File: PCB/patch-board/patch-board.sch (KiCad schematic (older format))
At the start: 104 parts, among them J1 USB_B, J11 AOUT1, J12 AOUT2, J13 AOUT3, J14 AOUT4, J15 AOUT5, J16 AOUT6, J17 AOUT7, J18 AOUT8, J2 LOGIC POWER SUPPLY, J21 DIGITAL OUT1, J22 DIGITAL OUT2, J23 DIGITAL OUT3, J24 DIGITAL OUT4, J3 MEGA_13-8, J31 S01, J32 S02, J33 S03, J34 S04, J35 S05, J36 S06, J37 S07, J38 S08, J39 S09, J4 MEGA_7-0, J40 S10, J41 SV, J42 SV, J43 SV, J44 SV, J45 SV, J46 SV, J5 MEGA_14-21, J6 MEGA_A8-A15, J7 MEGA_A0-A7, J8 MEGA_POWER, J9 MEGA_22-53, SW1 D1A, SW11 SW_DPST, SW12 SW_DPST, SW13 Conn_01x02, SW2 D1B, SW3 D2A, SW4 D2B, SW5 D3A, SW6 D3B, SW7 D4A, SW8 D4B, U1 74HC00, U10 74HC08, U11 74HC00, U12 74HC08, U13 74HC08, U2 74HC08, U3 74HC08, U4 74HC00, U5 74HC08, U6 74HC08, U7 74HC14, U8 74HC00, U9 74HC08

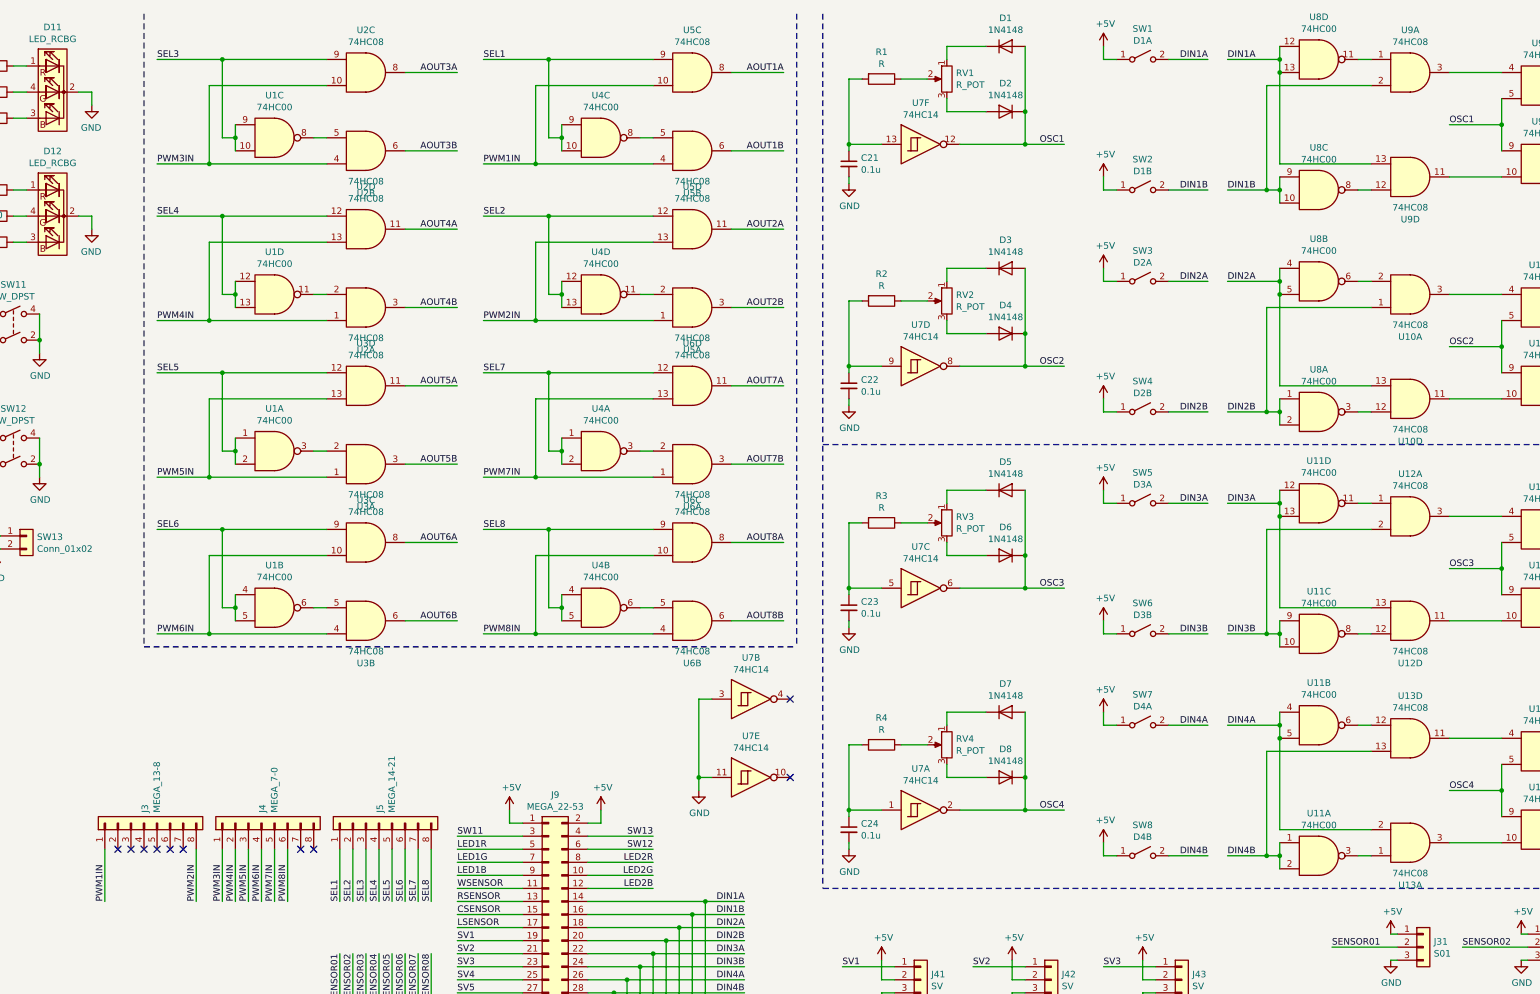
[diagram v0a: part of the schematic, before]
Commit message: D13 ピンの配線ミスを修正 AOUT5-8 のシルクミスを修正 U13 のユニット割り当てミスを修正
git-svn-id: https://shiro-home.ddns.net/svn/project/motor-driver/trunk@32 73406841-da20-4056-b287-c5b29fcc9b8e
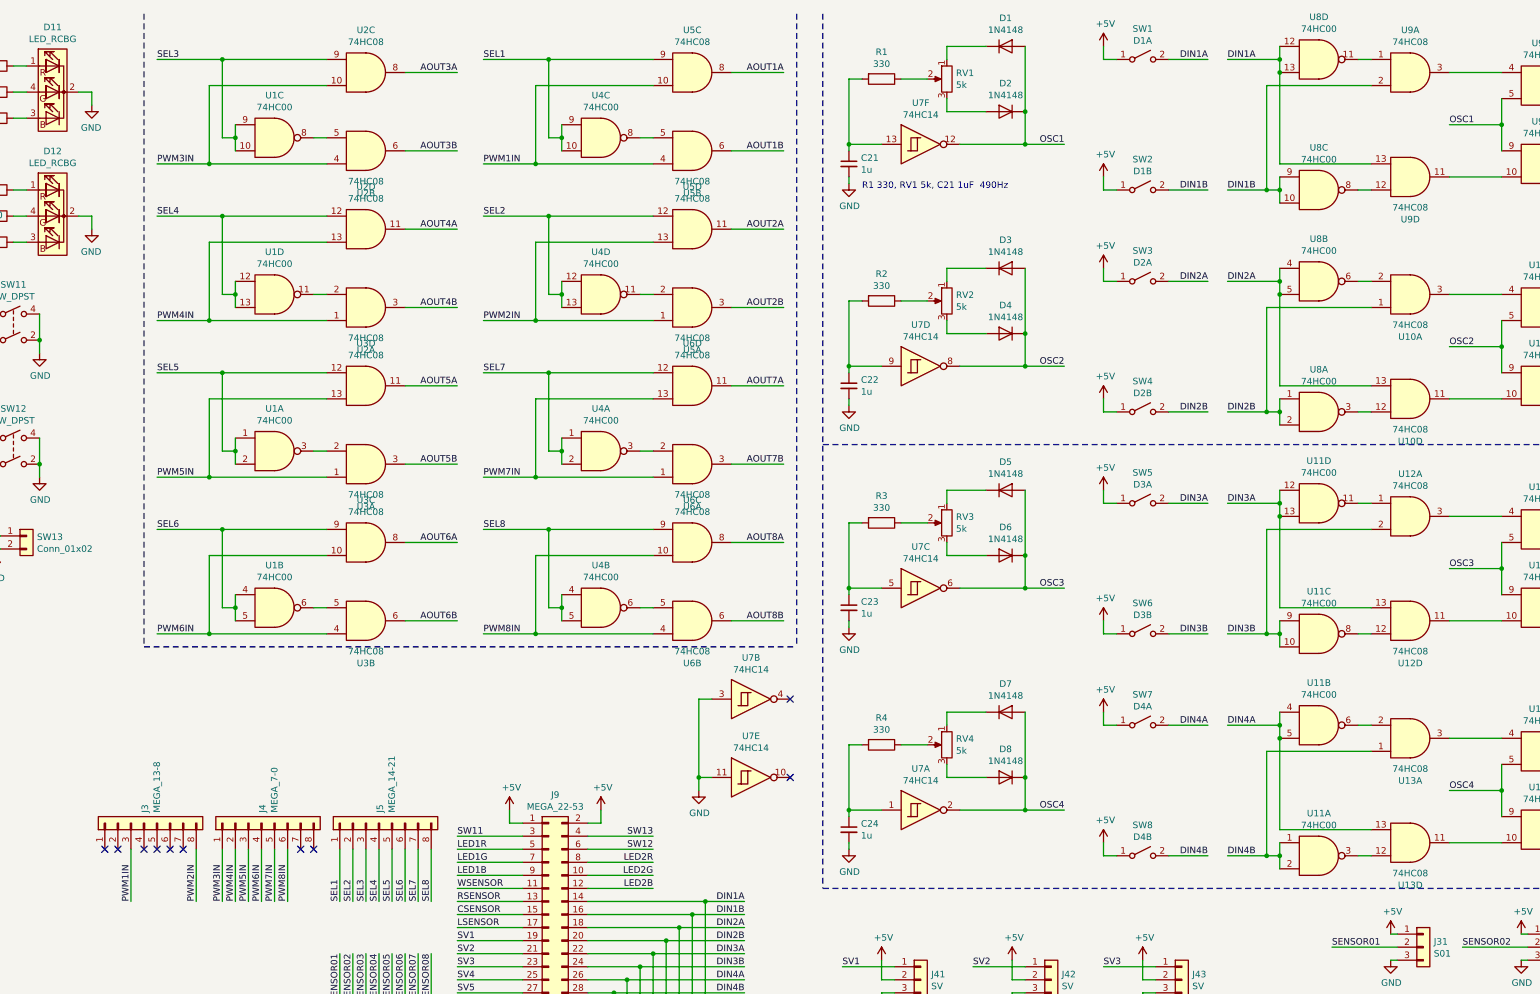
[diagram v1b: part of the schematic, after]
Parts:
- C21, C22, C23, C24: value 0.1u -> 1u
- R1, R2, R3, R4: value R -> 330
- RV1, RV2, RV3, RV4: value R_POT -> 5k
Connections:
- net DIN4A: now also U13.13; no longer U13.2
- net DIN4B: now also U13.1; no longer U13.13
- net PWM1IN: now also J3.3 (Pin_3); no longer J3.1 (Pin_1)
- net at U13.4: now also U13.3; no longer U13.11
- net at U11.3: now also U13.12; no longer U13.1
- net at U13.10: now also U13.11; no longer U13.3
- net at U11.6: now also U13.2; no longer U13.12
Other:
- note added: "R1 330, RV1 5k, C21 1uF 490Hz"
- moved on the sheet: U13A, U13D
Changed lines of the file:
@@
 P 8250 1100
 F 0 "R1" V 8043 1100 50  0000 C CNN
-F 1 "R" V 8134 1100 50  0000 C CNN
+F 1 "330" V 8134 1100 50  0000 C CNN
 F 2 "Resistor_THT:R_Axial_DIN0207_L6.3mm_D2.5mm_P10.16mm_Horizontal" V 8180 1100 50  0001 C CNN
 F 3 "~" H 8250 1100 50  0001 C CNN
@@
 P 8750 1100
 F 0 "RV1" H 8680 1146 50  0000 R CNN
-F 1 "R_POT" H 8680 1055 50  0000 R CNN
+F 1 "5k" H 8680 1055 50  0000 R CNN
 F 2 "MyLib:GF063P1" H 8750 1100 50  0001 C CNN
 F 3 "~" H 8750 1100 50  0001 C CNN
@@
 P 8250 2800
 F 0 "R2" V 8043 2800 50  0000 C CNN
-F 1 "R" V 8134 2800 50  0000 C CNN
+F 1 "330" V 8134 2800 50  0000 C CNN
 F 2 "Resistor_THT:R_Axial_DIN0207_L6.3mm_D2.5mm_P10.16mm_Horizontal" V 8180 2800 50  0001 C CNN
 F 3 "~" H 8250 2800 50  0001 C CNN
@@
 P 8750 2800
 F 0 "RV2" H 8680 2846 50  0000 R CNN
-F 1 "R_POT" H 8680 2755 50  0000 R CNN
+F 1 "5k" H 8680 2755 50  0000 R CNN
 F 2 "MyLib:GF063P1" H 8750 2800 50  0001 C CNN
 F 3 "~" H 8750 2800 50  0001 C CNN
@@
 P 8250 4500
 F 0 "R3" V 8043 4500 50  0000 C CNN
-F 1 "R" V 8134 4500 50  0000 C CNN
+F 1 "330" V 8134 4500 50  0000 C CNN
 F 2 "Resistor_THT:R_Axial_DIN0207_L6.3mm_D2.5mm_P10.16mm_Horizontal" V 8180 4500 50  0001 C CNN
 F 3 "~" H 8250 4500 50  0001 C CNN
@@
 P 8750 4500
 F 0 "RV3" H 8680 4546 50  0000 R CNN
-F 1 "R_POT" H 8680 4455 50  0000 R CNN
+F 1 "5k" H 8680 4455 50  0000 R CNN
 F 2 "MyLib:GF063P1" H 8750 4500 50  0001 C CNN
 F 3 "~" H 8750 4500 50  0001 C CNN
@@
 P 8250 6200
 F 0 "R4" V 8043 6200 50  0000 C CNN
-F 1 "R" V 8134 6200 50  0000 C CNN
+F 1 "330" V 8134 6200 50  0000 C CNN
 F 2 "Resistor_THT:R_Axial_DIN0207_L6.3mm_D2.5mm_P10.16mm_Horizontal" V 8180 6200 50  0001 C CNN
 F 3 "~" H 8250 6200 50  0001 C CNN
@@
 P 8750 6200
 F 0 "RV4" H 8680 6246 50  0000 R CNN
-F 1 "R_POT" H 8680 6155 50  0000 R CNN
+F 1 "5k" H 8680 6155 50  0000 R CNN
 F 2 "MyLib:GF063P1" H 8750 6200 50  0001 C CNN
 F 3 "~" H 8750 6200 50  0001 C CNN
@@
 Wire Wire Line
 	4200 7000 4200 7400
-Text Label 2300 7400 1    50   ~ 0
+Text Label 2500 7400 1    50   ~ 0
 PWM1IN
 Wire Wire Line
@@
 $EndComp
 Wire Wire Line
-	2300 7000 2300 7400
+	2500 7000 2500 7400
 Text Label 4500 7400 1    50   ~ 0
 SEL5
@@
 $EndComp
 NoConn ~ 2400 7000
-NoConn ~ 2500 7000
+NoConn ~ 2300 7000
 NoConn ~ 2600 7000
 NoConn ~ 2700 7000
@@
 P 8000 1750
 F 0 "C21" H 8092 1796 50  0000 L CNN
-F 1 "0.1u" H 8092 1705 50  0000 L CNN
+F 1 "1u" H 8092 1705 50  0000 L CNN
 F 2 "Capacitor_THT:C_Disc_D3.4mm_W2.1mm_P2.50mm" H 8000 1750 50  0001 C CNN
 F 3 "~" H 8000 1750 50  0001 C CNN
@@
 P 8000 3450
 F 0 "C22" H 8092 3496 50  0000 L CNN
-F 1 "0.1u" H 8092 3405 50  0000 L CNN
+F 1 "1u" H 8092 3405 50  0000 L CNN
 F 2 "Capacitor_THT:C_Disc_D3.4mm_W2.1mm_P2.50mm" H 8000 3450 50  0001 C CNN
 F 3 "~" H 8000 3450 50  0001 C CNN
@@
 P 8000 5150
 F 0 "C23" H 8092 5196 50  0000 L CNN
-F 1 "0.1u" H 8092 5105 50  0000 L CNN
+F 1 "1u" H 8092 5105 50  0000 L CNN
 F 2 "Capacitor_THT:C_Disc_D3.4mm_W2.1mm_P2.50mm" H 8000 5150 50  0001 C CNN
 F 3 "~" H 8000 5150 50  0001 C CNN
@@
 P 8000 6850
 F 0 "C24" H 8092 6896 50  0000 L CNN
-F 1 "0.1u" H 8092 6805 50  0000 L CNN
+F 1 "1u" H 8092 6805 50  0000 L CNN
 F 2 "Capacitor_THT:C_Disc_D3.4mm_W2.1mm_P2.50mm" H 8000 6850 50  0001 C CNN
 F 3 "~" H 8000 6850 50  0001 C CNN
@@
 L 74xx:74LS08 U13
 U 1 1 5F77F572
+P 12300 6150
+F 0 "U13" H 12300 6475 50  0000 C CNN
+F 1 "74HC08" H 12300 6384 50  0000 C CNN
+F 2 "Package_SO:SO-14_5.3x10.2mm_P1.27mm" H 12300 6150 50  0001 C CNN
+F 3 "https://assets.nexperia.com/documents/data-sheet/74HC_HCT04.pdf" H 12300 6150 50  0001 C CNN
+	1    12300 6150
+	1    0    0    1
+$EndComp
+$Comp
+L 74xx:74LS08 U13
+U 4 1 5F77F590
 P 12300 6950
 F 0 "U13" H 12300 7275 50  0000 C CNN
@@
 F 2 "Package_SO:SO-14_5.3x10.2mm_P1.27mm" H 12300 6950 50  0001 C CNN
 F 3 "https://assets.nexperia.com/documents/data-sheet/74HC_HCT04.pdf" H 12300 6950 50  0001 C CNN
-	1    12300 6950
+	4    12300 6950
 	1    0    0    1
 $EndComp
-$Comp
-L 74xx:74LS08 U13
-U 4 1 5F77F590
-P 12300 6150
-F 0 "U13" H 12300 6475 50  0000 C CNN
-F 1 "74HC08" H 12300 6384 50  0000 C CNN
-F 2 "Package_SO:SO-14_5.3x10.2mm_P1.27mm" H 12300 6150 50  0001 C CNN
-F 3 "https://assets.nexperia.com/documents/data-sheet/74HC_HCT04.pdf" H 12300 6150 50  0001 C CNN
-	4    12300 6150
-	1    0    0    -1
-$EndComp
 Wire Wire Line
 	4400 7800 4400 8300
@@
 	0    -1   1    0
 $EndComp
+Text Notes 8100 1950 0    50   ~ 0
+R1 330, RV1 5k, C21 1uF  490Hz
 $EndSCHEMATC
